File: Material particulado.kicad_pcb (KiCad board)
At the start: 2 copper layers, 4 parts, among them U1 ESP32-S3-WROOM-1, U2 LM35-D, U3 LM358_DFN, U4 LM358_DFN

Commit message: Editando Huellas
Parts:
- moved U1 4.90 mm to (49.5, 44.1)
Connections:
- U1 pad 12: unconnected-(U1-IO8-Pad12) -> Net-(U1-IO8)
- U1 pad 17: unconnected-(U1-IO9-Pad17) -> Net-(U1-IO9)
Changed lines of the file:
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@@
 	(footprint "RF_Module:ESP32-S3-WROOM-1"
 		(layer "F.Cu")
-		(at 49.25 39.26)
+		(at 49.5 44.15)
 		(descr "2.4 GHz Wi-Fi and Bluetooth module  https://www.espressif.com/sites/default/files/documentation/esp32-s3-wroom-1_wroom-1u_datasheet_en.pdf")
 		(tags "2.4 GHz Wi-Fi and Bluetooth module")
@@
 			(size 1.5 0.9)
 			(layers "F.Cu" "F.Mask" "F.Paste")
-			(net "unconnected-(U1-IO8-Pad12)")
+			(net "Net-(U1-IO8)")
 			(pinfunction "IO8_12")
 			(pintype "bidirectional")
@@
 			(size 1.5 0.9)
 			(layers "F.Cu" "F.Mask" "F.Paste")
-			(net "unconnected-(U1-IO9-Pad17)")
+			(net "Net-(U1-IO9)")
 			(pinfunction "IO9_17")
 			(pintype "bidirectional")
@@
 			(polygon
 				(pts
-					(xy 25.25 32.51) (xy 73.25 32.51) (xy 73.25 11.51) (xy 25.25 11.51)
+					(xy 25.5 37.4) (xy 73.5 37.4) (xy 73.5 16.4) (xy 25.5 16.4)
 				)
 			)

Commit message: Organizando Huellas y smd -yara
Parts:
- added C1: 1uf, Capacitor_SMD:C_0805_2012Metric, F.Cu at (28.5, 91.5)
- added R1: 15k, Resistor_SMD:R_0805_2012Metric_Pad1.20x1.40mm_HandSolder, F.Cu at (18.5, 80.5)
- added R2: 2.2k, Resistor_SMD:R_0805_2012Metric, F.Cu at (54.1, 99.0)
- added R3: 2.2k, Resistor_SMD:R_0805_2012Metric, F.Cu at (56.2, 78.5)
- added R4: 1k, Resistor_SMD:R_0805_2012Metric_Pad1.20x1.40mm_HandSolder, F.Cu at (32.0, 104.0)
- added U5: ~, 0.96huella:Sin título, F.Cu at (40.2, 36.5)
- moved U1 15.0 mm to (64.5, 43.1)
- moved U2 14.8 mm to (19.0, 57.5)

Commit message: Corte cables
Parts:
- moved U2 3.35 mm to (17.5, 60.5)
- moved R4 1.90 mm to (32.0, 105.9), turned to 180 degrees
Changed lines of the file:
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@@
 	(footprint "Package_SO:SOIC-8_3.9x4.9mm_P1.27mm"
 		(layer "F.Cu")
-		(at 19 57.5)
+		(at 17.5 60.5)
 		(descr "SOIC, 8 Pin (JEDEC MS-012AA, https://www.analog.com/media/en/package-pcb-resources/package/pkg_pdf/soic_narrow-r/r_8.pdf)")
 		(tags "SOIC SO")
@@
 			(at 0 1.65 0)
 			(layer "F.Fab")
+			(hide yes)
 			(effects
 				(font
@@
 			(at 0 2 0)
 			(layer "F.Fab")
+			(hide yes)
 			(effects
 				(font
@@
 	(footprint "Resistor_SMD:R_0805_2012Metric_Pad1.20x1.40mm_HandSolder"
 		(layer "F.Cu")
-		(at 32 104)
+		(at 32 105.9 180)
 		(descr "Resistor SMD 0805 (2012 Metric), square (rectangular) end terminal, IPC-7351 nominal with elongated pad for handsoldering. (Body size source: IPC-SM-782 page 72, https://www.pcb-3d.com/wordpress/wp-content/uploads/ipc-sm-782a_amendment_1_and_2.pdf)")
 		(tags "resistor handsolder")
@@
 		(duplicate_pad_numbers_are_jumpers no)
 		(fp_line
+			(start -0.227064 0.735)
+			(end 0.227064 0.735)
+			(stroke
+				(width 0.12)
+				(type solid)
+			)
+			(layer "F.SilkS")
+		)
+		(fp_line
 			(start -0.227064 -0.735)
 			(end 0.227064 -0.735)
-			(stroke
-				(width 0.12)
-				(type solid)
-			)
-			(layer "F.SilkS")
-		)
-		(fp_line
-			(start -0.227064 0.735)
-			(end 0.227064 0.735)
 			(stroke
 				(width 0.12)
@@
 		)
 		(pad "1" smd roundrect
-			(at -1 0)
+			(at -1 0 180)
 			(size 1.2 1.4)
 			(layers "F.Cu" "F.Mask" "F.Paste")
@@
 		)
 		(pad "2" smd roundrect
-			(at 1 0)
+			(at 1 0 180)
 			(size 1.2 1.4)
 			(layers "F.Cu" "F.Mask" "F.Paste")
@@
 		)
 	)
+	(segment
+		(start 18.6 79.815256)
+		(end 18.915256 79.5)
+		(width 0.2)
+		(layer "F.Cu")
+		(net "Net-(U4A-+)")
+	)
 	(embedded_fonts no)

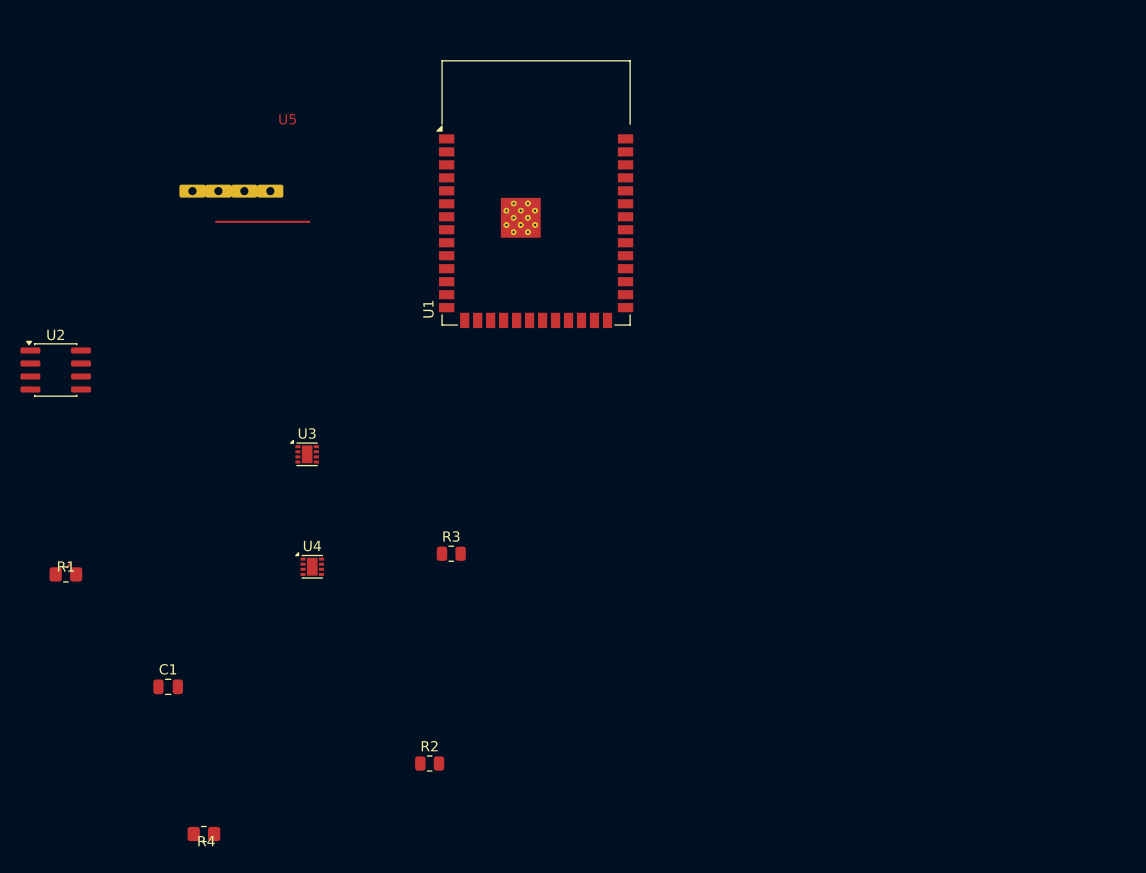
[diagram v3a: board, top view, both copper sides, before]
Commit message: Hice cambios en las huellas
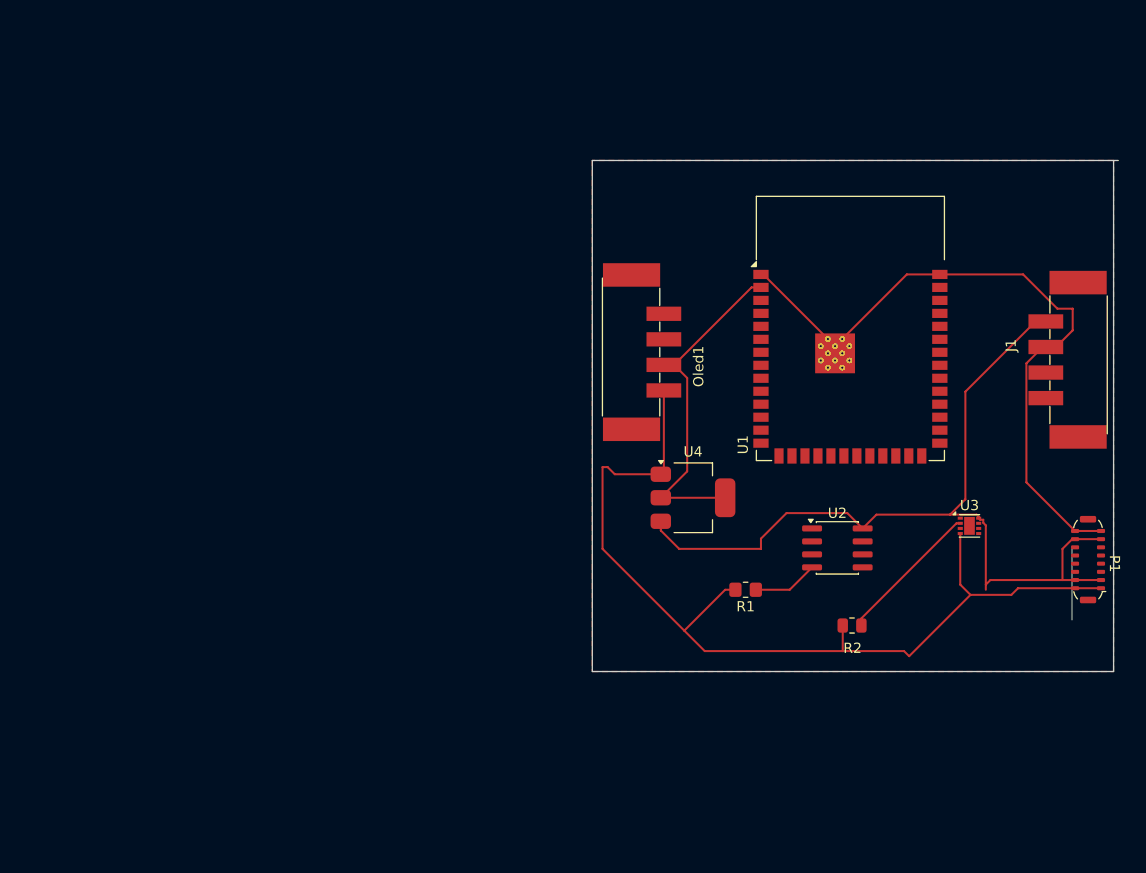
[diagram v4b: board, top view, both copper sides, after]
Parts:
- removed C1: 1uf, Capacitor_SMD:C_0805_2012Metric
- removed R3: 2.2k, Resistor_SMD:R_0805_2012Metric
- removed R4: 1k, Resistor_SMD:R_0805_2012Metric_Pad1.20x1.40mm_HandSolder
- removed U5: ~, 0.96huella:Sin título
- added J1: PMS, TerminalBlock_Phoenix:TerminalBlock_Phoenix_PTSM-0,5-4-2,5-V-SMD_1x04-1MP_P2.50mm_Vertical, F.Cu at (116.5, 59.5)
- added Oled1: ~, TerminalBlock_Phoenix:TerminalBlock_Phoenix_PTSM-0,5-4-2,5-V-SMD_1x04-1MP_P2.50mm_Vertical, F.Cu at (74.9, 58.8)
- added P1: USB_C_Plug_USB2.0, Connector_USB:USB_C_Plug_ShenzhenJingTuoJin_918-118A2021Y40002_Vertical, F.Cu at (118.5, 79.0)
- U4: value LM358_DFN -> Regulador de 5v a 3.3v; footprint Package_DFN_QFN:DFN-8-1EP_2x2mm_P0.5mm_EP1.05x1.75mm -> Package_TO_SOT_SMD:SOT-223-3_TabPin2
- moved U2 78.4 mm to (94.0, 77.9)
- moved R1 66.5 mm to (85.0, 82.0), turned to 180 degrees
- moved U3 65.2 mm to (106.9, 75.8)
- moved R2 43.5 mm to (95.4, 85.5), turned to 180 degrees
- moved U4 37.9 mm to (79.8, 73.0)
- moved U1 33.5 mm to (95.2, 56.4)
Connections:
- R1 pad 2: GNDREF -> GND
- R2 pad 2: GNDREF -> GND
- U1 pad 1: GNDREF -> GND
- U1 pad 12: Net-(U1-IO8) -> SDA
- U1 pad 17: Net-(U1-IO9) -> SCK
- U1 pad 2: Net-(U1-3V3) -> +3V3
- U1 pad 32: Net-(U1-IO39) -> Vout(LM35)
- U1 pad 36: unconnected-(U1-RXD0-Pad36) -> TX(PMS)
- U1 pad 37: unconnected-(U1-TXD0-Pad37) -> RX(PMS)
- U1 pad 40: GNDREF -> GND
- U1 pad 41: GNDREF -> GND
- U2 pad 1: Net-(U1-IO39) -> 32(I039)
- U2 pad 8: Net-(U1-3V3) -> +5V
- U3 pad 1: Net-(U4A-+) -> Salida
- U3 pad 4: GNDREF -> GND
- U3 pad 8: Net-(U1-3V3) -> +5V
- U4 pad 1: Net-(U4A--) -> GND
- U4 pad 2: Net-(U4A--) -> +3V3
- U4 pad 3: Net-(U4A-+) -> +5V
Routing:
- net GND: track 0.00 -> 159.8 mm
- net +5V: track 0.00 -> 85.7 mm
- net +3V3: track 0.00 -> 33.5 mm
- net Net-(U3A--): track 0.00 -> 14.2 mm
- net unconnected-(P1-SHIELD-PadSH): track 0.00 -> 6.89 mm
- net Net-(U2-GND): track 0.00 -> 6.41 mm
- added copper zone on F.Cu, net GND
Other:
- board outline added: 51.5 x 50 mm

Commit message: cambie pistas-yara
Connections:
- U1 pad 36: TX(PMS) -> RX(D0)
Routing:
- net +5V: track 85.7 -> 104.5 mm
- net RX(D0): track 0.00 -> 13.3 mm
- net RX(PMS): track 0.00 -> 12.8 mm
- net GND: track 159.8 -> 163.7 mm
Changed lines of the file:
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@@
 			(size 1.5 0.9)
 			(layers "F.Cu" "F.Mask" "F.Paste")
-			(net "TX(PMS)")
+			(net "RX(D0)")
 			(pinfunction "RXD0_36")
 			(pintype "bidirectional")
@@
 	)
 	(segment
+		(start 115.89 59.47)
+		(end 117 60.58)
+		(width 0.2)
+		(layer "F.Cu")
+		(net "+5V")
+	)
+	(segment
 		(start 94.95 74.5)
 		(end 89 74.5)
@@
 	)
 	(segment
+		(start 116 65)
+		(end 108.5 65)
+		(width 0.2)
+		(layer "F.Cu")
+		(net "+5V")
+	)
+	(segment
 		(start 106.5 62.62)
 		(end 106.5 73.15)
@@
 	)
 	(segment
+		(start 117 60.58)
+		(end 117 64)
+		(width 0.2)
+		(layer "F.Cu")
+		(net "+5V")
+	)
+	(segment
 		(start 108.5 81.5)
 		(end 108.5 75.7)
@@
 	)
 	(segment
-		(start 113.37 55.75)
-		(end 106.5 62.62)
-		(width 0.2)
-		(layer "F.Cu")
-		(net "+5V")
-	)
-	(segment
 		(start 107.8 75)
 		(end 107.8 74.85)
@@
 	)
 	(segment
+		(start 117 64)
+		(end 116 65)
+		(width 0.2)
+		(layer "F.Cu")
+		(net "+5V")
+	)
+	(segment
 		(start 96.45 76)
 		(end 94.95 74.5)
@@
 	)
 	(segment
+		(start 114.37 55.75)
+		(end 111.25 55.75)
+		(width 0.2)
+		(layer "F.Cu")
+		(net "+5V")
+	)
+	(segment
 		(start 116.95 77.05)
 		(end 116 78)
@@
 	)
 	(segment
+		(start 112.47 59.47)
+		(end 115.89 59.47)
+		(width 0.2)
+		(layer "F.Cu")
+		(net "+5V")
+	)
+	(segment
 		(start 116 81.05)
 		(end 117.23 81.05)
@@
 	)
 	(segment
+		(start 110 57)
+		(end 112.47 59.47)
+		(width 0.2)
+		(layer "F.Cu")
+		(net "+5V")
+	)
+	(segment
 		(start 116 78)
 		(end 116 81.05)
@@
 	)
 	(segment
+		(start 111.25 55.75)
+		(end 110 57)
+		(width 0.2)
+		(layer "F.Cu")
+		(net "+5V")
+	)
+	(segment
+		(start 108.5 65)
+		(end 106.5 63)
+		(width 0.2)
+		(layer "F.Cu")
+		(net "+5V")
+	)
+	(segment
 		(start 96.325 84.8)
 		(end 105.625 75.5)
@@
 	)
 	(segment
+		(start 115.37 58.25)
+		(end 118 60.88)
+		(width 0.2)
+		(layer "F.Cu")
+		(net "GND")
+	)
+	(segment
 		(start 94.5 88)
 		(end 94.5 85.5)
@@
 	)
 	(segment
+		(start 112.49 71.51)
+		(end 117.23 76.25)
+		(width 0.2)
+		(layer "F.Cu")
+		(net "GND")
+	)
+	(segment
 		(start 83 82)
 		(end 84 82)
@@
 	)
 	(segment
+		(start 118 60.88)
+		(end 118 64)
+		(width 0.2)
+		(layer "F.Cu")
+		(net "GND")
+	)
+	(segment
 		(start 111.65 81.85)
 		(end 111 82.5)
@@
 	)
 	(segment
-		(start 112.47 59.85)
-		(end 112.47 71.49)
+		(start 114.3 65.7)
+		(end 112.49 67.51)
+		(width 0.2)
+		(layer "F.Cu")
+		(net "GND")
+	)
+	(segment
+		(start 116.3 65.7)
+		(end 114.3 65.7)
 		(width 0.2)
 		(layer "F.Cu")
@@
 	)
 	(segment
+		(start 112.49 67.51)
+		(end 112.49 71.51)
+		(width 0.2)
+		(layer "F.Cu")
+		(net "GND")
+	)
+	(segment
 		(start 101 88.5)
 		(end 100.5 88)
@@
 	)
 	(segment
-		(start 114.07 58.25)
-		(end 112.47 59.85)
-		(width 0.2)
-		(layer "F.Cu")
-		(net "GND")
-	)
-	(segment
 		(start 112.47 71.49)
-		(end 117.23 76.25)
+		(end 112.49 71.51)
+		(width 0.2)
+		(layer "F.Cu")
+		(net "GND")
+	)
+	(segment
+		(start 118 64)
+		(end 116.3 65.7)
 		(width 0.2)
 		(layer "F.Cu")
@@
 		(net "unconnected-(P1-SHIELD-PadSH)")
 	)
+	(segment
+		(start 104.3 56.23)
+		(end 111.32 63.25)
+		(width 0.2)
+		(layer "F.Cu")
+		(net "RX(D0)")
+	)
+	(segment
+		(start 104 56.23)
+		(end 104.3 56.23)
+		(width 0.2)
+		(layer "F.Cu")
+		(net "RX(D0)")
+	)
+	(segment
+		(start 111.32 63.25)
+		(end 114.37 63.25)
+		(width 0.2)
+		(layer "F.Cu")
+		(net "RX(D0)")
+	)
+	(segment
+		(start 112.75 60.75)
+		(end 114.37 60.75)
+		(width 0.2)
+		(layer "F.Cu")
+		(net "RX(PMS)")
+	)
+	(segment
+		(start 106.96 54.96)
+		(end 112.75 60.75)
+		(width 0.2)
+		(layer "F.Cu")
+		(net "RX(PMS)")
+	)
+	(segment
+		(start 104 54.96)
+		(end 106.96 54.96)
+		(width 0.2)
+		(layer "F.Cu")
+		(net "RX(PMS)")
+	)
 	(zone
